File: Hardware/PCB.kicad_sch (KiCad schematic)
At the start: 18 parts, among them J2 Conn_01x06, Q1 Q_NMOS, SW2 SW_Push, U1 ME54BS01_V1.0, U3 MCP1700x-330xxTT

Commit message: WIP
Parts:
- added C4, C5: 100nF, Capacitor_SMD:C_0805_2012Metric, symbol Device:C
- C3: value C -> 100nF
- Q1: symbol Device:Q_NMOS -> Transistor_FET:Q_NMOS_GSD
- R1: footprint Resistor_SMD:R_0805_2012Metric_Pad1.20x1.40mm_HandSolder -> Resistor_SMD:R_0805_2012Metric
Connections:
- net -BATT is gone; now on net GND: Batt1.2 (Pin_2)
- net +BATT: now also Q1.3 (D); no longer Q1.D
- net BATT_M: no longer U1.7 (P1.14/AIN7)
- net BATT_M_CTRL: now also Q1.1 (G), U1.7 (P1.14/AIN7); no longer Q1.G
- net GND: now also Probe2.1 (Pin_1), C4.2, C5.2; no longer Probe2.2 (Pin_2)
- net PROBE_1_DIVIDER: now also C5.1
- net PROBE_2_DIVIDER: now also Probe2.2 (Pin_2), C4.1; no longer Probe2.1 (Pin_1)
- net at R4.2: now also Q1.2 (S); no longer Q1.S
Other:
- moved on the sheet: Probe2, R2

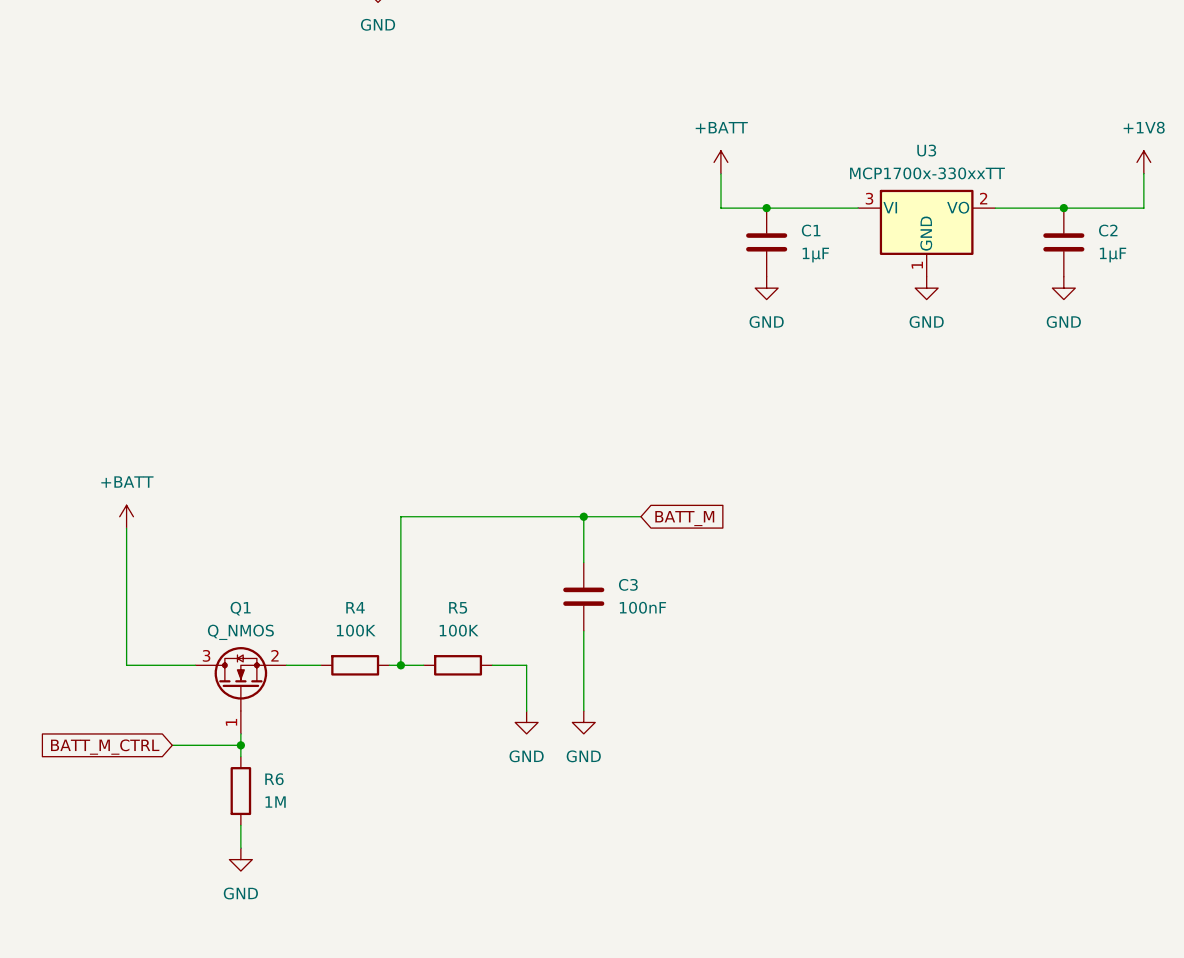
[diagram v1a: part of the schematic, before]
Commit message: WIP Finished outline with LDO
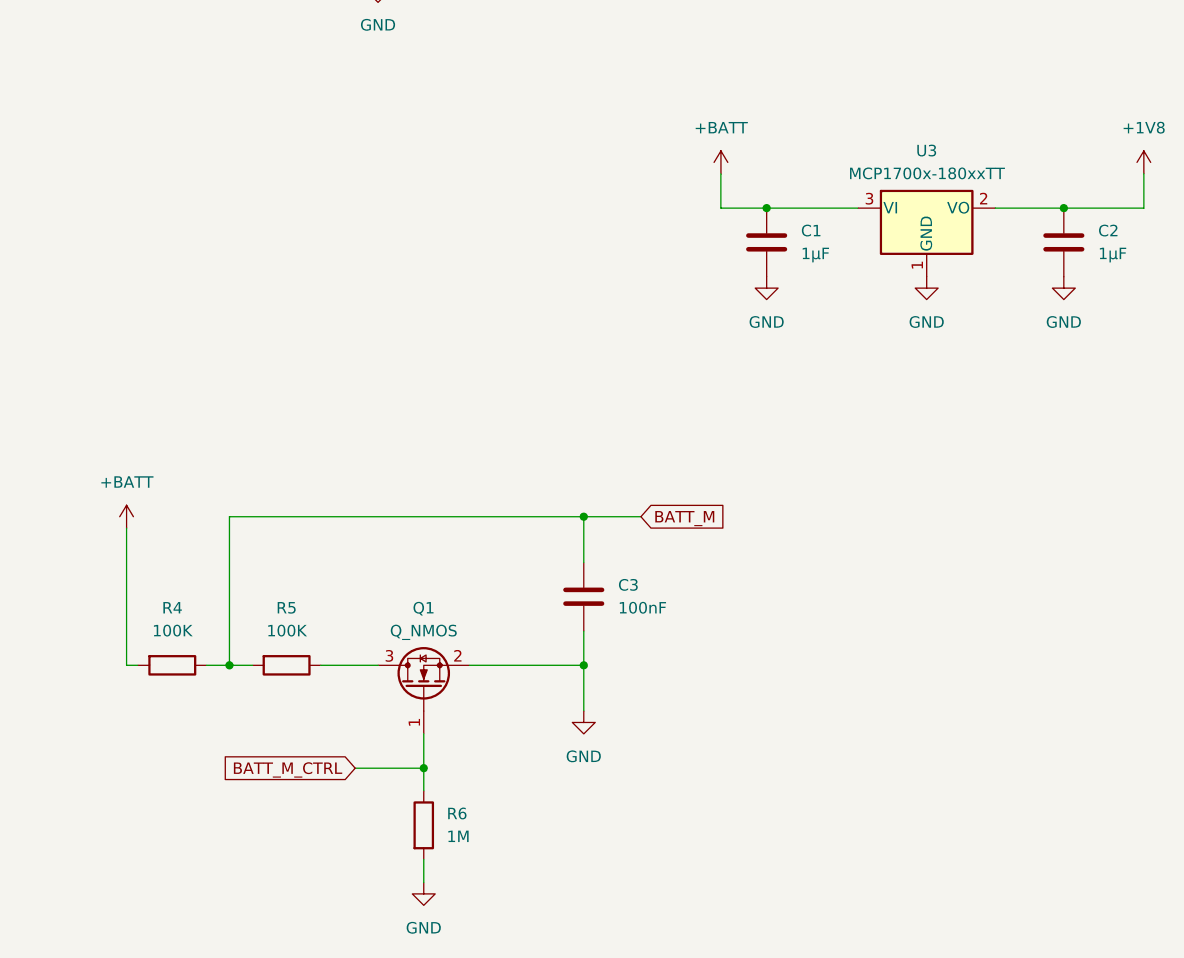
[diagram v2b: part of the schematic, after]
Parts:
- U3: value MCP1700x-330xxTT -> MCP1700x-180xxTT; symbol Regulator_Linear:MCP1700x-330xxTT -> Regulator_Linear:MCP1700x-180xxTT
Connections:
- net +BATT: now also R4.2; no longer Q1.3 (D)
- net GND: now also Q1.2 (S); no longer R5.1
- new net: Q1.3 (D), R5.1
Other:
- moved on the sheet: Q1, R4, R5, R6
